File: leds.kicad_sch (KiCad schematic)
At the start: 17 parts, among them Q1 Si2301CDS, Q2 2N7002

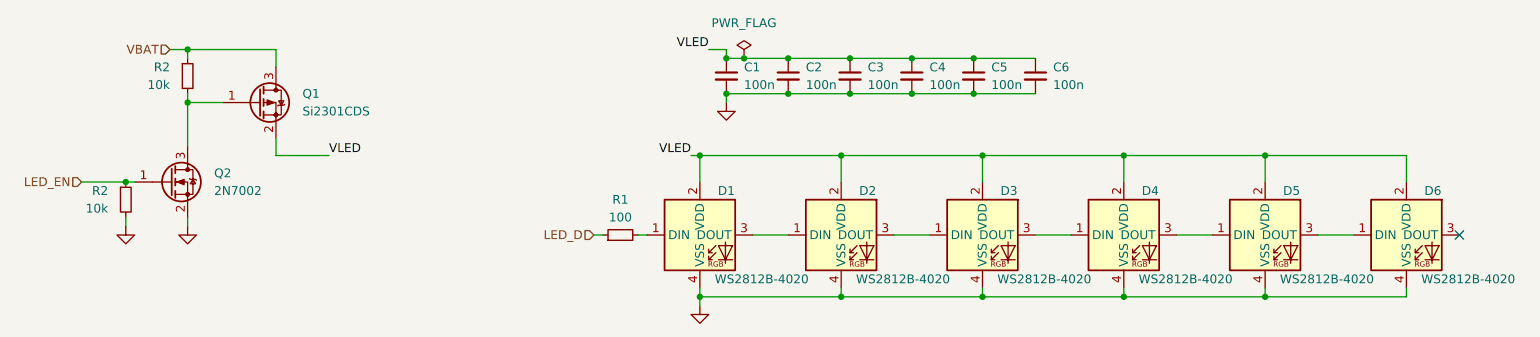
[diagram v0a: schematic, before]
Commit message: Use bare ESP32 chip instead of module (#1)
* fixed library issues

* add submodules to CI/CD

* fix yaml syntax

* added part numbers

* Bare ESP layout

* fix erc/drc

* fix overlap

* added part numbers

* fixed layout
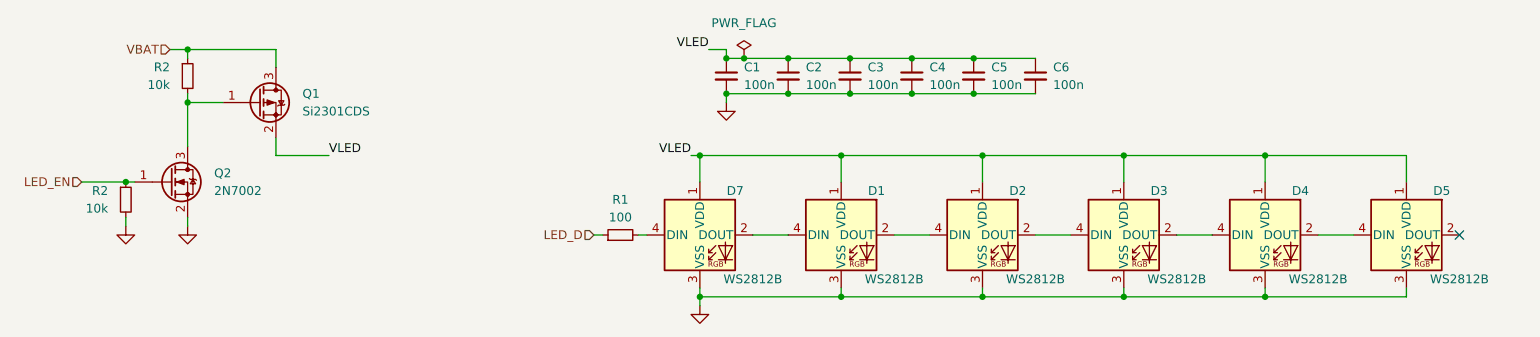
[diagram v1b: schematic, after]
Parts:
- removed D1, D2, D3, D4, D5, D6: WS2812B-4020, WS2812B-4020:WS2812B-4020, symbol WS2812B-4020:WS2812B-4020
- added D1, D2, D3, D4, D5, D7: WS2812B, LED_SMD:LED_WS2812B_PLCC4_5.0x5.0mm_P3.2mm, symbol LED:WS2812B
- C1, C2, C3, C4, C5, C6: LCSC (none) -> C1525
- Q1: LCSC (none) -> C10487
- Q2: LCSC (none) -> C8545
- R1: footprint Capacitor_SMD:C_0402_1005Metric -> Resistor_SMD:R_0402_1005Metric; LCSC (none) -> C25076
- R2: footprint Capacitor_SMD:C_0402_1005Metric -> Resistor_SMD:R_0402_1005Metric; LCSC (none) -> C25086
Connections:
- net GND: now also D1.3 (VSS), D2.3 (VSS), D3.3 (VSS), D4.3 (VSS), D5.3 (VSS), D7.3 (VSS)
- net VLED: now also D1.1 (VDD), D2.1 (VDD), D3.1 (VDD), D4.1 (VDD), D5.1 (VDD), D7.1 (VDD)
- net at R1.2: now also D7.4 (DIN)
- new net: D1.2 (DOUT), D2.4 (DIN)
- new net: D1.4 (DIN), D7.2 (DOUT)
- new net: D4.2 (DOUT), D5.4 (DIN)
- new net: D2.2 (DOUT), D3.4 (DIN)
- new net: D3.2 (DOUT), D4.4 (DIN)
